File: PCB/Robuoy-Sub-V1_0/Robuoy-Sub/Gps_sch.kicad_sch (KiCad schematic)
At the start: 4 parts, among them J501 GPS, U4 USBLC6-4SC6

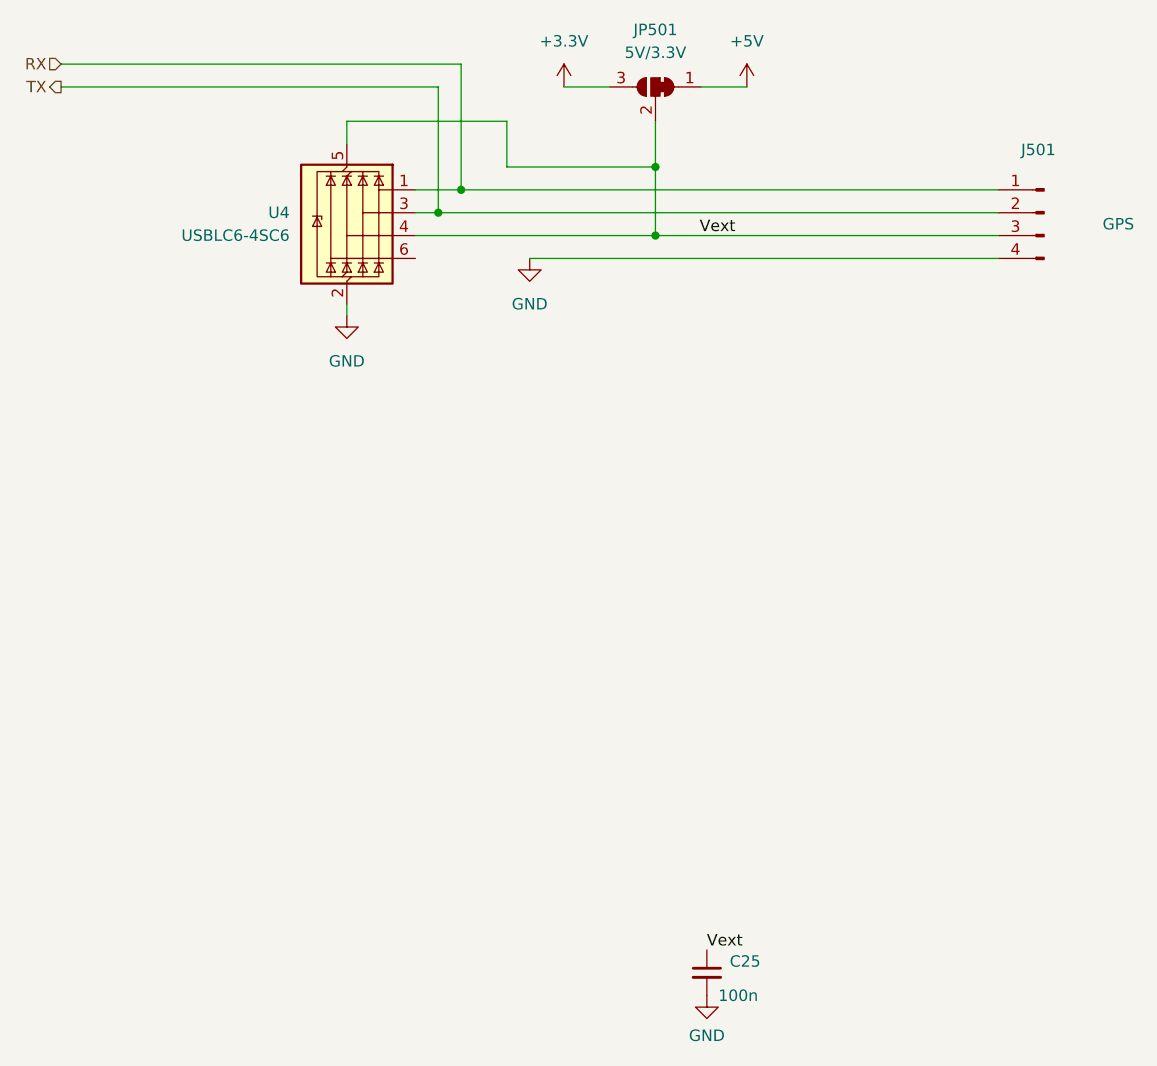
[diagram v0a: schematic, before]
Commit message: PCB names changed. Cost calculation added
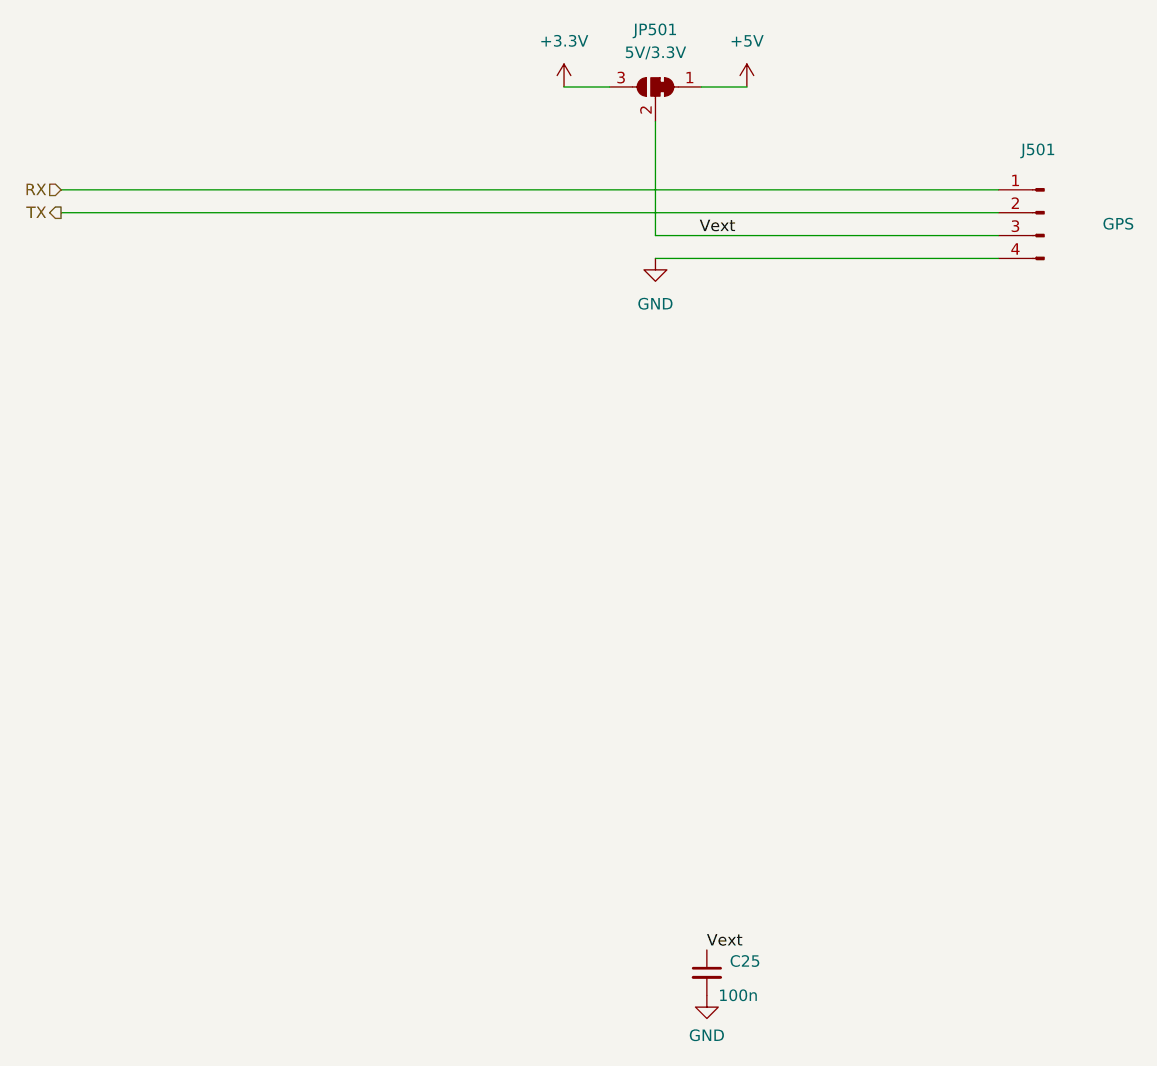
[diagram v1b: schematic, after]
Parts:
- removed U4: USBLC6-4SC6, Package_TO_SOT_SMD:SOT-23-6, symbol Power_Protection:USBLC6-4SC6
